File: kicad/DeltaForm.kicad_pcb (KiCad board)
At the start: 2 copper layers, 85.4 x 128.6 mm, 82 parts

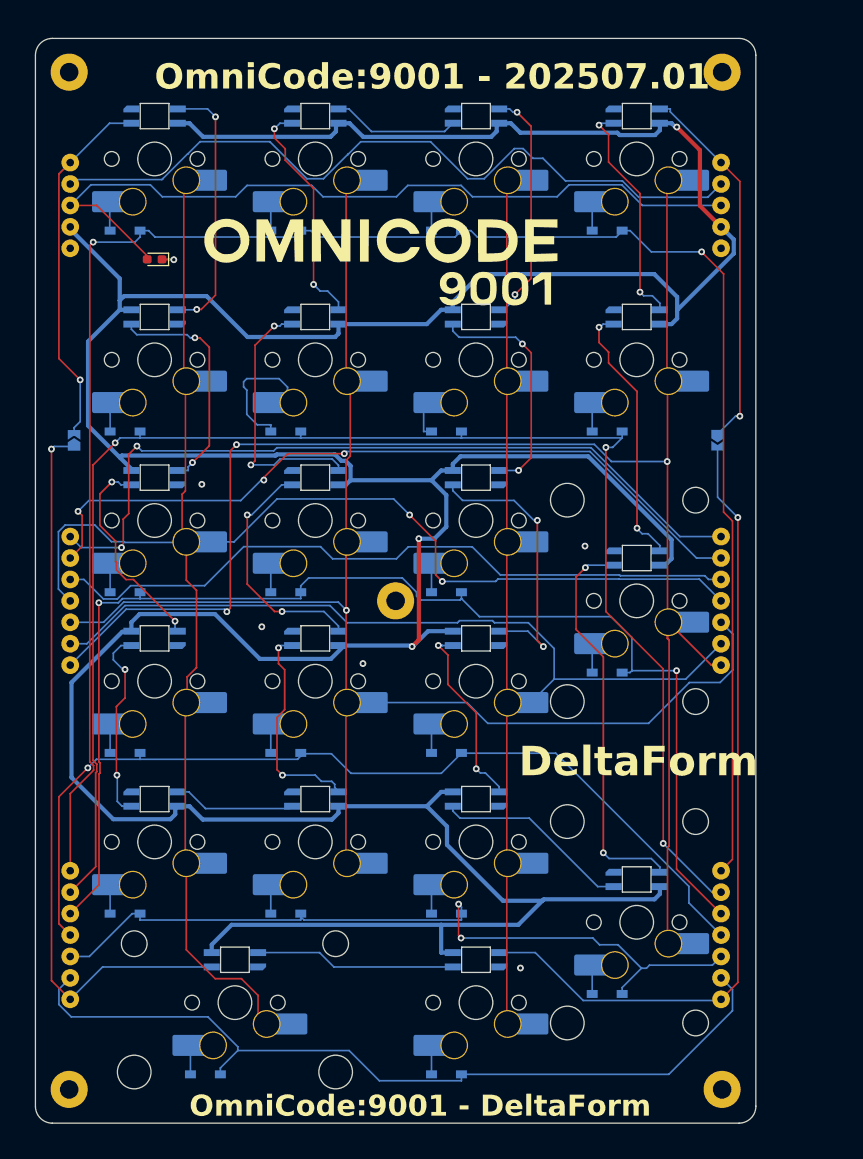
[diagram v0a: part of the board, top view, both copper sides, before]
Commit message: more tweaks  (#3)
* small tweaks

* GlyphMatrix - 3mm screws

* PhaseShift - 3mm screws

* DeltaForm - 3mm screws

* updated README.md
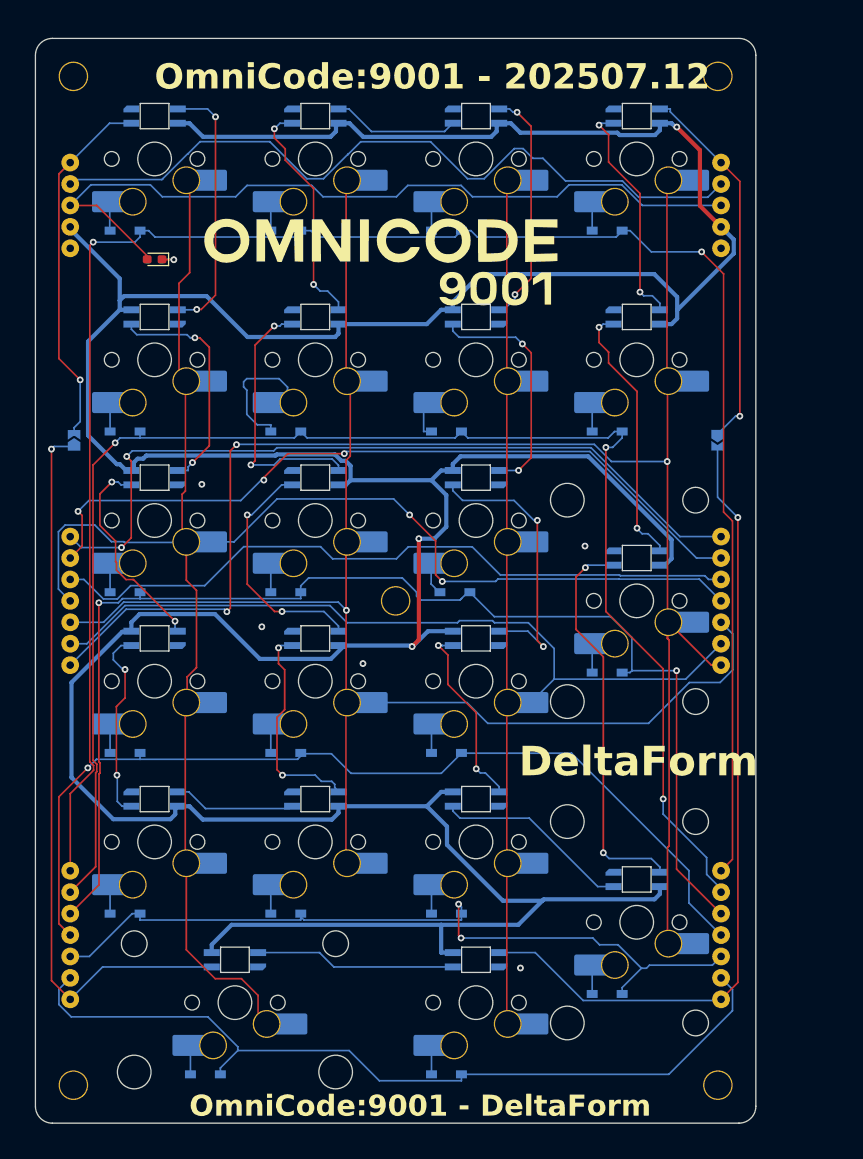
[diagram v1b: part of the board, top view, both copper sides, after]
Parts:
- H1, H2, H3, H4, H5: value MountingHole_2.2mm_M2_Pad -> MountingHole_3.2mm_Pad; footprint TB2086_MISC:MountingHole_2.2mm_M2_Pad -> TB2086_MISC:MountingHole_3.2mm_Pad
- moved D11 1.00 mm to (212.9, 141.4)
- moved H1 0.71 mm to (167.7, 80.2)
- moved H2 0.71 mm to (244.1, 80.2)
- moved H3 0.71 mm to (244.1, 199.8)
- moved H4 0.71 mm to (167.7, 199.8)
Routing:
- net COL3: track 215.0 -> 217.4 mm
- net ROW15: track 110.7 -> 111.8 mm
- net Net-(D11-A): track 6.12 -> 6.63 mm
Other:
- board text added: "OmniCode:9001 - 202507.12"
- board text removed: "OmniCode:9001 - 202507.01"

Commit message: more updates (#12)
* working on kibot

* added position file

* fixed footprint for PhaseShift and DeltaForm

* fixed footprint side for GlyphMatrix

* KiBot: changed BOM type

* added fonts

* KiBot

* refreshed submodule

* updated footprint for GlyphMatrix

* updated footprint for PhaseShift

* updated footprint for DeltaForm

* updated build guide
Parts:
- S1, S10, S11, S12, S13, S14, S15, S16, S17, S18, S19, S2, S20, S21, S3, S4, S5, S6, S7, S8, S9: moved to B.Cu
- turned S1 to 0 degrees
- turned S10 to 0 degrees
- turned S11 to 0 degrees
- turned S12 to 0 degrees
- turned S13 to 0 degrees
- turned S14 to 0 degrees
- turned S15 to 0 degrees
- turned S16 to 0 degrees
- turned S17 to 0 degrees
- turned S18 to 0 degrees
- turned S19 to 0 degrees
- turned S2 to 0 degrees
- turned S20 to 0 degrees
- turned S21 to 0 degrees
- turned S3 to 0 degrees
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
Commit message: updated fonts (#13)
* Changed fonts for silk screen

* updated fonts for PhaseShift

* updated fonts for DeltaForm

* updated kibot for GlyphMatrix

* added dummy schematic files for GlyphMatrix

* updated kibot config

* added PhaseShift to workflow

* added DeltaForm to workflow
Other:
- board text added: "OmniCode:9001 - 202507.22"
- board text removed: "OmniCode:9001 - 202507.12"

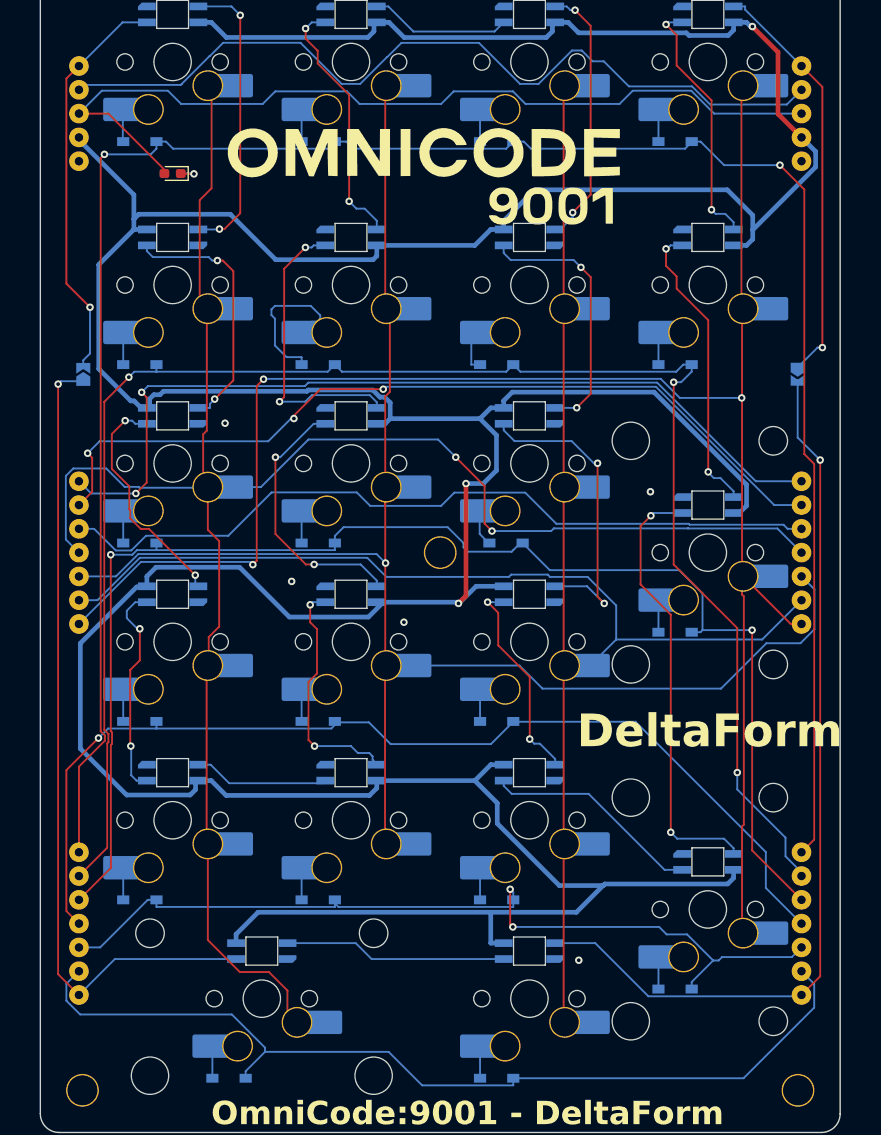
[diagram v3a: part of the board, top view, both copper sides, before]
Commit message: adjusted positions
- pogo pins
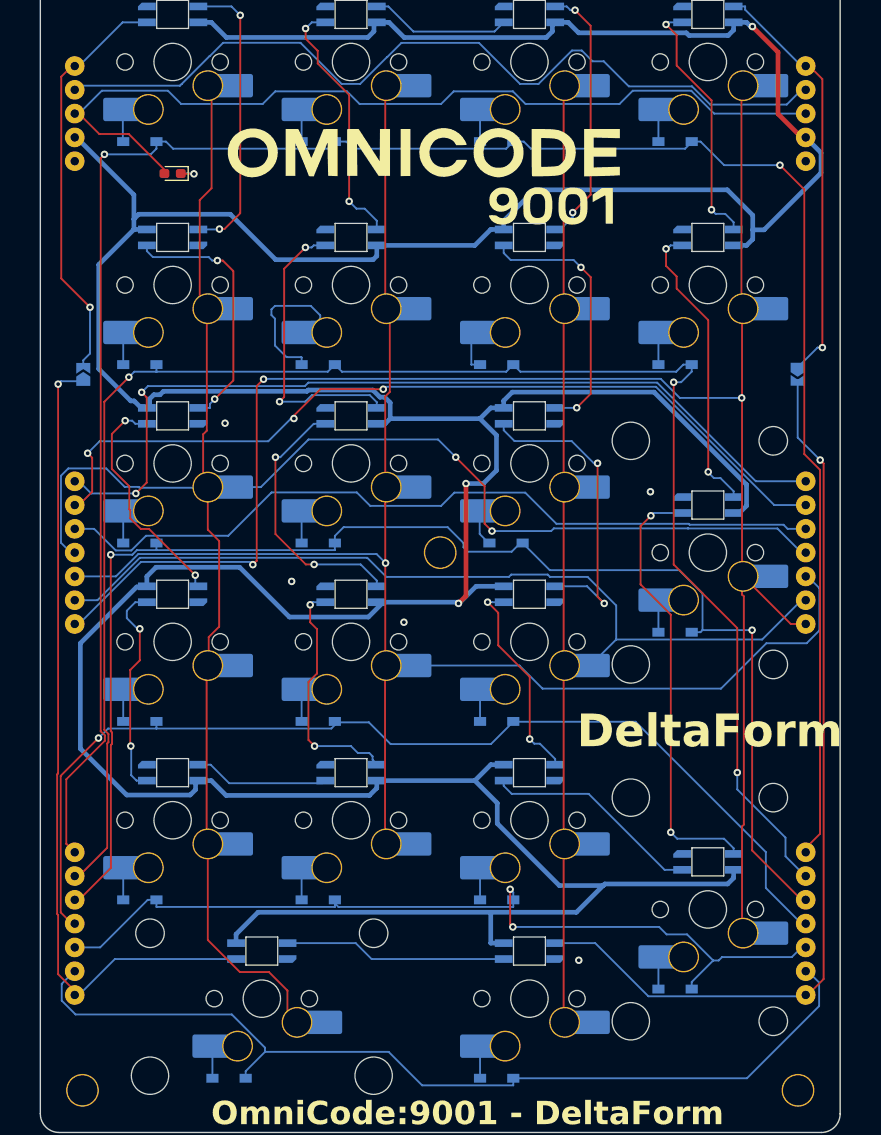
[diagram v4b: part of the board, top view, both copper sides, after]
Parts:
- moved POGO1 0.45 mm to (166.8, 95.5)
- moved POGO2 0.45 mm to (244.9, 95.5)
- moved POGO3 0.45 mm to (166.8, 142.4)
- moved POGO4 0.45 mm to (244.9, 142.4)
- moved POGO5 0.45 mm to (166.8, 182.0)
- moved POGO6 0.45 mm to (244.9, 182.0)
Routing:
- net COL3: track 217.4 -> 214.5 mm
- net ROW12: track 227.8 -> 229.2 mm
- net ROW13: track 180.9 -> 179.6 mm
- net ROW17: track 99.6 -> 100.4 mm
- net COL4: track 182.6 -> 183.2 mm

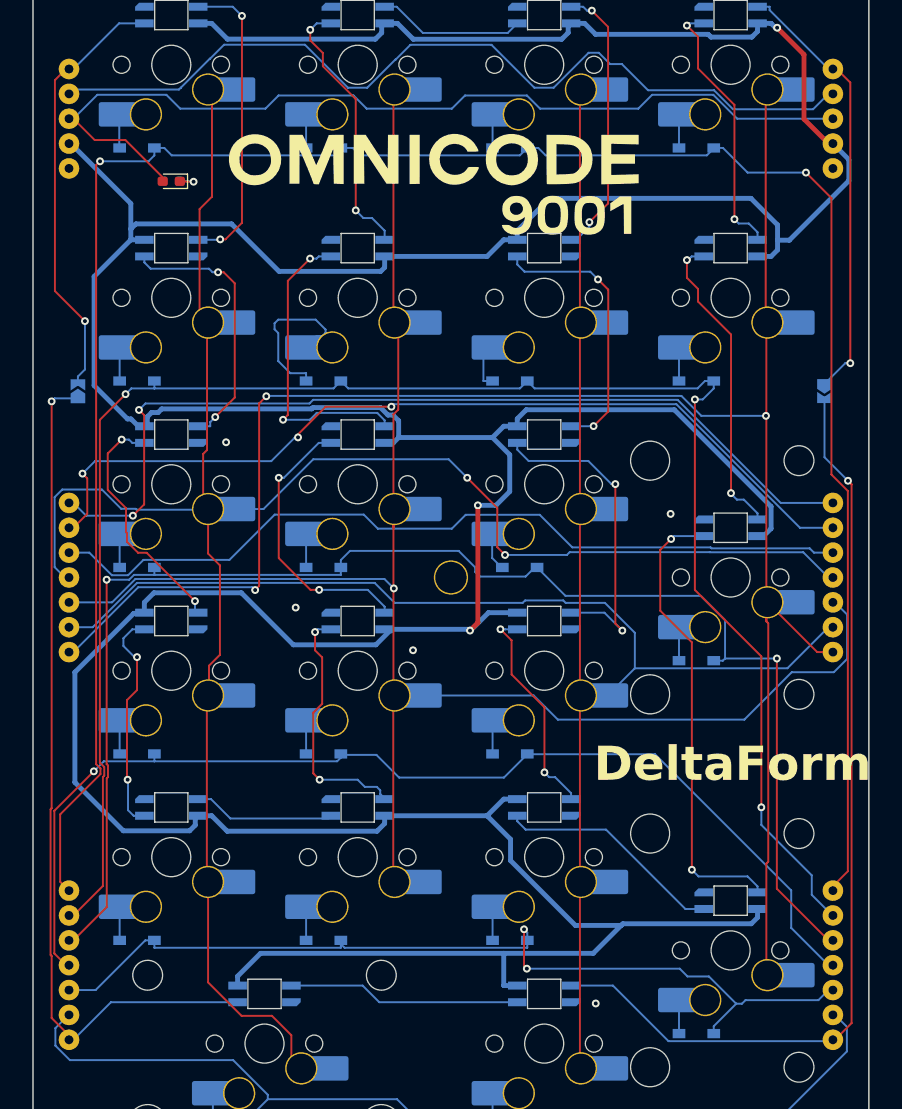
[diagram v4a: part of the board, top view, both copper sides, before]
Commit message: small tweak
- pogo pin
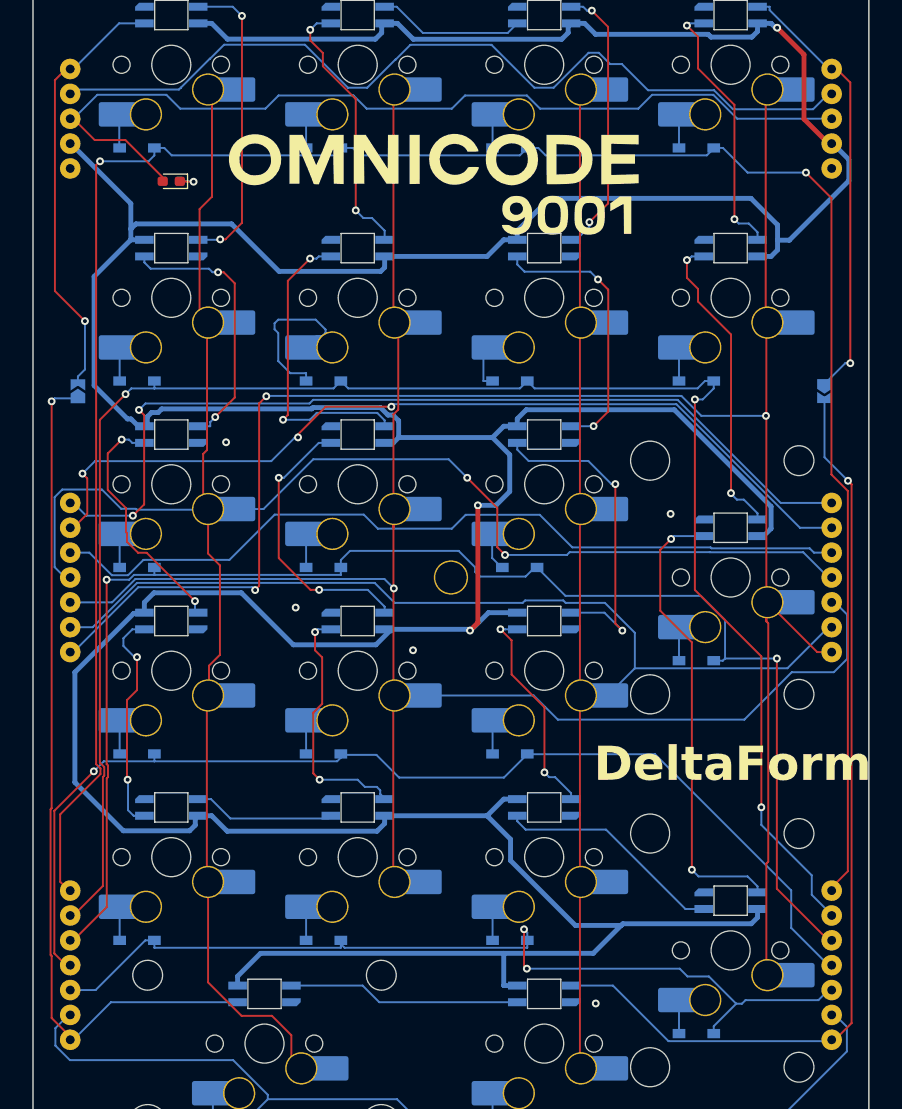
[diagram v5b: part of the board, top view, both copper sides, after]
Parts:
- moved POGO1 0.12 mm to (167.0, 95.5)
- moved POGO2 0.12 mm to (244.8, 95.5)
- moved POGO3 0.12 mm to (167.0, 142.4)
- moved POGO4 0.12 mm to (244.8, 142.4)
- moved POGO5 0.12 mm to (167.0, 182.0)
- moved POGO6 0.12 mm to (244.8, 182.0)
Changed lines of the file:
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@@
 	(footprint "TB2086_MISC:Pogopin_1x05_P2.54mm_Curved"
 		(layer "B.Cu")
-		(at 244.9 95.5125 -90)
+		(at 244.775 95.5125 -90)
 		(property "Reference" "POGO2"
 			(at 0 -1.77 180)
@@
 	(footprint "TB2086_MISC:Pogopin_1x07_P2.54mm_Curved"
 		(layer "B.Cu")
-		(at 244.9 142.3875 -90)
+		(at 244.775 142.3875 -90)
 		(property "Reference" "POGO4"
 			(at 0 -1.77 180)
@@
 	(footprint "TB2086_MISC:Pogopin_1x07_P2.54mm_Curved"
 		(layer "B.Cu")
-		(at 244.9 182 -90)
+		(at 244.775 182 -90)
 		(property "Reference" "POGO6"
 			(at 0 -1.77 180)
@@
 	(footprint "TB2086_MISC:Pogopin_1x07_P2.54mm_Curved"
 		(layer "B.Cu")
-		(at 166.85 182 90)
+		(at 166.975 182 90)
 		(property "Reference" "POGO5"
 			(at 0 -1.77 180)
@@
 	(footprint "TB2086_MISC:Pogopin_1x07_P2.54mm_Curved"
 		(layer "B.Cu")
-		(at 166.85 142.3875 90)
+		(at 166.975 142.3875 90)
 		(property "Reference" "POGO3"
 			(at 0 -1.77 180)
@@
 	(footprint "TB2086_MISC:Pogopin_1x05_P2.54mm_Curved"
 		(layer "B.Cu")
-		(at 166.85 95.5125 90)
+		(at 166.975 95.5125 90)
 		(property "Reference" "POGO1"
 			(at 0 -1.77 180)

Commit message: 202508.04
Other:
- board text added: "OmniCode:9001 - 202508.04"
- board text removed: "OmniCode:9001 - 202507.22"

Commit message: tweaked zone (#22)
* small tweak

* removed isolated copper islands
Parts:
- moved G*** 0.22 mm to (204.4, 101.6)
- turned POGO1 to -90 degrees
- turned POGO2 to 90 degrees
- turned POGO3 to -90 degrees
- turned POGO4 to 90 degrees
- turned POGO5 to -90 degrees
- turned POGO6 to 90 degrees
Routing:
- net Net-(D4-A): track 18.1 -> 5.11 mm
- net ROW16: track 93.2 -> 88.1 mm, vias 2 -> 0
- net NUM: track 94.2 -> 98.1 mm
- net COL2: track 83.5 -> 87.1 mm
- net Net-(L17-DOUT): track 23.3 -> 26.7 mm
- net Net-(L11-DOUT): track 33.4 -> 30.2 mm
- net COL5: track 205.9 -> 209.2 mm
- net Net-(L7-DIN): track 27.3 -> 29.7 mm
- net Net-(L3-DIN): track 27.5 -> 25.2 mm
- net +5V: track 505.3 -> 507.4 mm, vias 3 -> 13
- net Net-(L12-DOUT): track 23.2 -> 21.2 mm
- net SCR: track 88.7 -> 86.8 mm
- net ROW13: track 179.6 -> 181.5 mm
- net COL0: track 93.4 -> 95.2 mm
- net Net-(L2-DOUT): track 27.6 -> 29.1 mm
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
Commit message: quick fix
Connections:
- POGO3 pad 5: COL4 -> COL6
- POGO3 pad 7: COL6 -> COL4
- POGO4 pad 1: COL6 -> COL4
- POGO4 pad 3: COL4 -> COL6
- S10 pad 2: COL4 -> COL6
- S13 pad 2: COL4 -> COL6
- S16 pad 2: COL4 -> COL6
- S19 pad 2: COL6 -> COL4
- S20 pad 2: COL6 -> COL4
- S3 pad 2: COL4 -> COL6
- S4 pad 2: COL4 -> COL6
- S7 pad 2: COL6 -> COL4
- S8 pad 2: COL6 -> COL4
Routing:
- net COL6: track 205.4 -> 183.9 mm, vias 3 -> 1
- net COL4: track 183.9 -> 205.4 mm, vias 1 -> 3
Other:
- board text added: "OmniCode:9001 - 202509.17"
- board text removed: "OmniCode:9001 - 202508.04"
